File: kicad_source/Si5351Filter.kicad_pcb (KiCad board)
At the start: 2 copper layers, 50 x 50 mm, 31 parts, among them CN1 CON-SMA-EDGE-S-ND, CN2 CON-SMA-EDGE-S-ND, CN3 CON-SMA-EDGE-S-ND, CN4 CON-SMA-EDGE-S-ND, CN5 CON-SMA-EDGE-S-ND, CN6 CON-SMA-EDGE-S-ND

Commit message: added dual footprint for big and small SMA connectors
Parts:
- CN1, CN2, CN3, CN4, CN5, CN6: footprint CON_wuerth:WR-SMA-PCB -> CON_wuerth:WR-SMA-PCB_dual
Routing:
- net GND: track 42.6 -> 107.6 mm, vias 22 -> 28

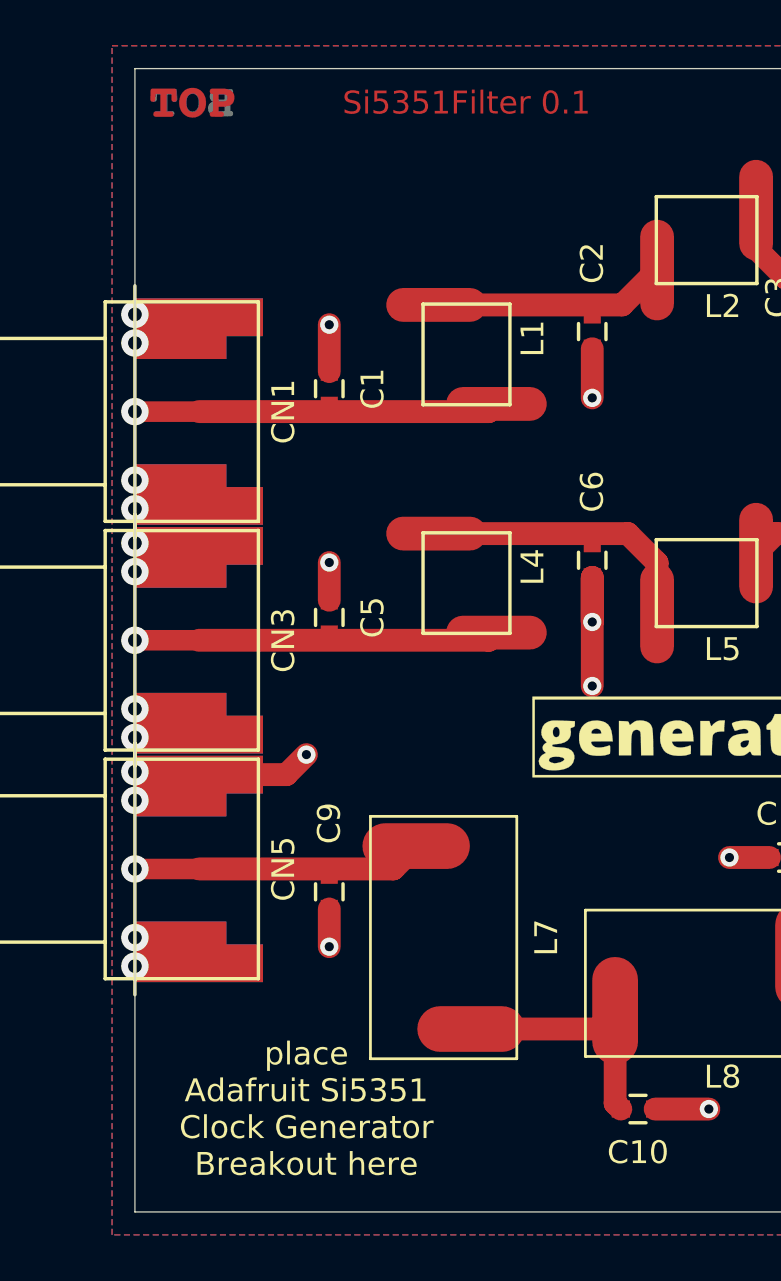
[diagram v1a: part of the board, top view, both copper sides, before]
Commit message: added holes for mounting and grounding
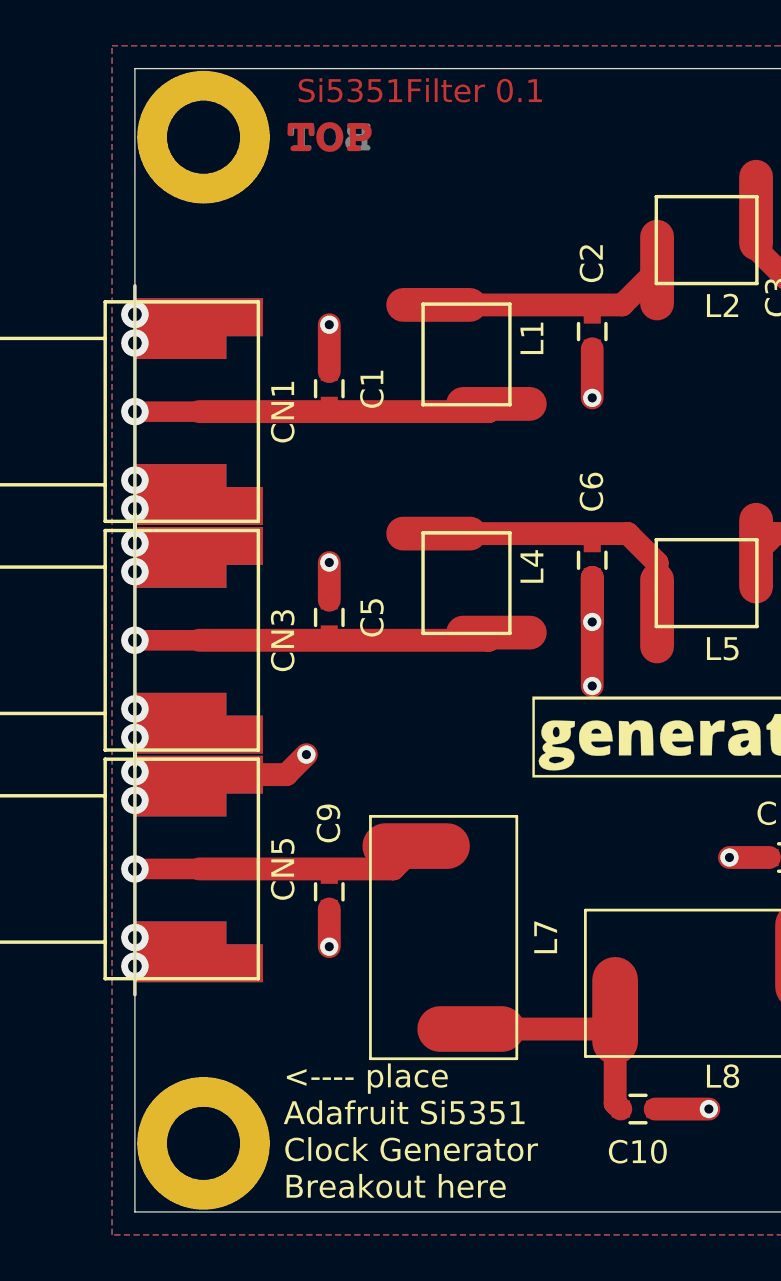
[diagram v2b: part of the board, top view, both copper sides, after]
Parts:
- added MECH1: MHP_3.2_5.8, MECH_mounting_holes:MHP_3.2_5.8, F.Cu at (103.0, 123.0)
- added MECH2: MHP_3.2_5.8, MECH_mounting_holes:MHP_3.2_5.8, F.Cu at (103.0, 167.0)
- moved L10 6.18 mm to (108.5, 123.0)
- moved L12 6.18 mm to (108.5, 123.0)
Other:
- board text added: "<---- place Adafruit Si5351 Clock Generator Breakout here"
- board text removed: "place Adafruit Si5351 Clock Generator Breakout here"

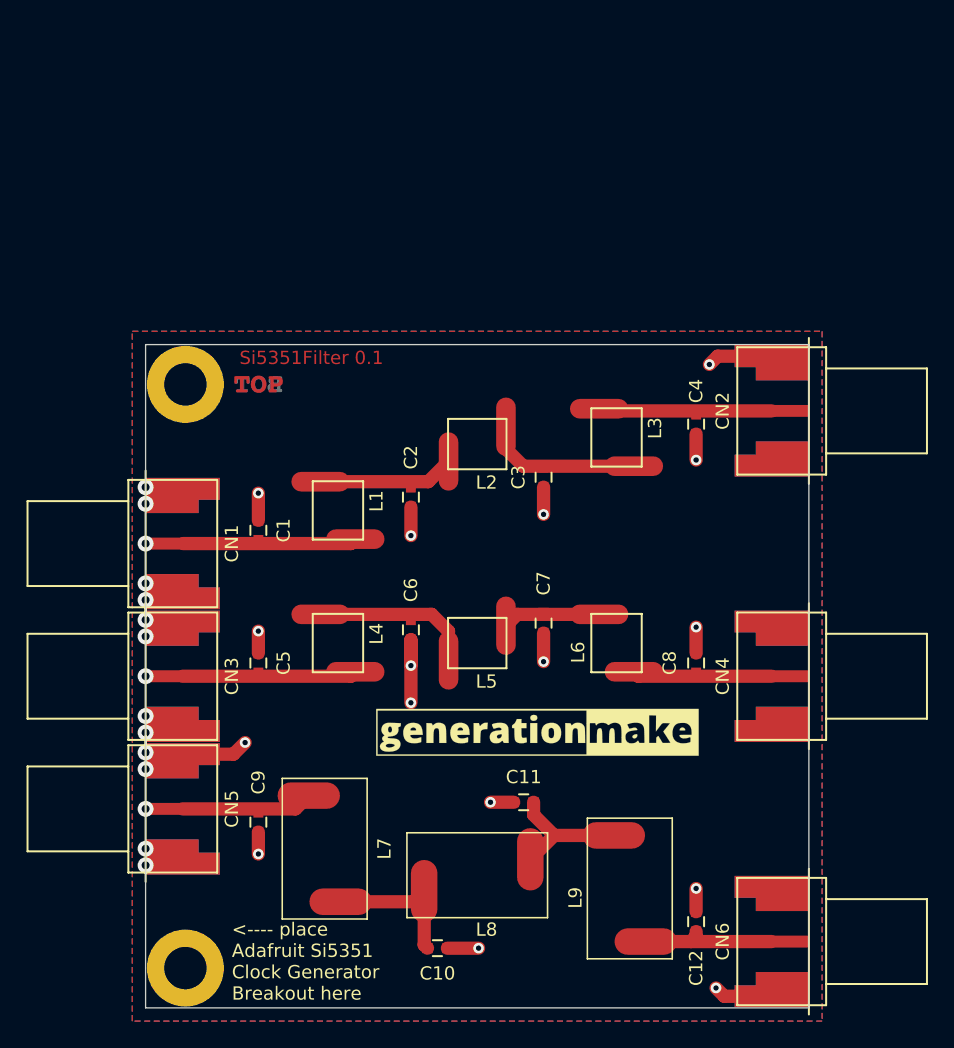
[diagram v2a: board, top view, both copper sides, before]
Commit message: updated castellated holes
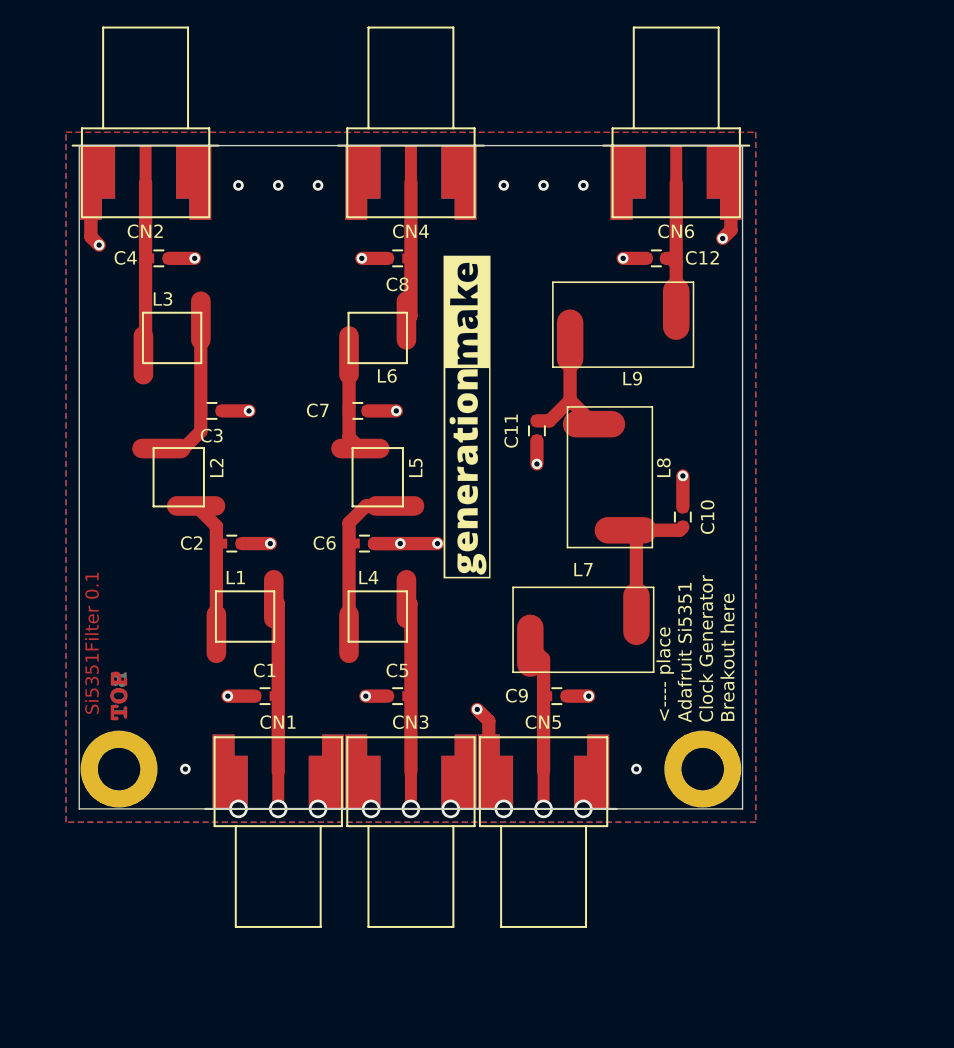
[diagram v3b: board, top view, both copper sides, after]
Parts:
- moved CN6 60.8 mm to (140.0, 105.0), turned to 180 degrees
- moved CN2 53.9 mm to (100.0, 105.0), turned to 180 degrees
- moved C12 50.1 mm to (138.5, 113.5), turned to 0 degrees
- moved CN4 50.0 mm to (120.0, 105.0), turned to 180 degrees
- moved L9 42.5 mm to (136.0, 118.5), turned to 0 degrees
- moved C4 42.4 mm to (101.0, 113.5), turned to 180 degrees
- moved MECH2 41.8 mm to (142.0, 152.0), turned to 90 degrees
- moved C8 37.9 mm to (119.0, 113.5), turned to 0 degrees
- moved C10 37.4 mm to (140.5, 133.0), turned to 270 degrees
- moved L3 34.3 mm to (102.0, 119.5), turned to 180 degrees
- moved L8 31.6 mm to (135.0, 130.0), turned to 90 degrees
- moved CN5 30.0 mm to (130.0, 155.0), turned to 0 degrees
- moved MECH1 29.4 mm to (98.0, 152.0), turned to 90 degrees
- moved L6 29.2 mm to (117.5, 119.5), turned to 0 degrees
- moved L13 29.0 mm to (129.5, 125.5), turned to 90 degrees
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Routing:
- net GND: vias 28 -> 30
